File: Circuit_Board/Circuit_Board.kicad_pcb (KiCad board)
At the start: 2 copper layers, 17 parts, among them J1 Conn_01x02, J2 Control stuff, J3 Power stuff, J4 Conn_02x06_Odd_Even, U1 Pico

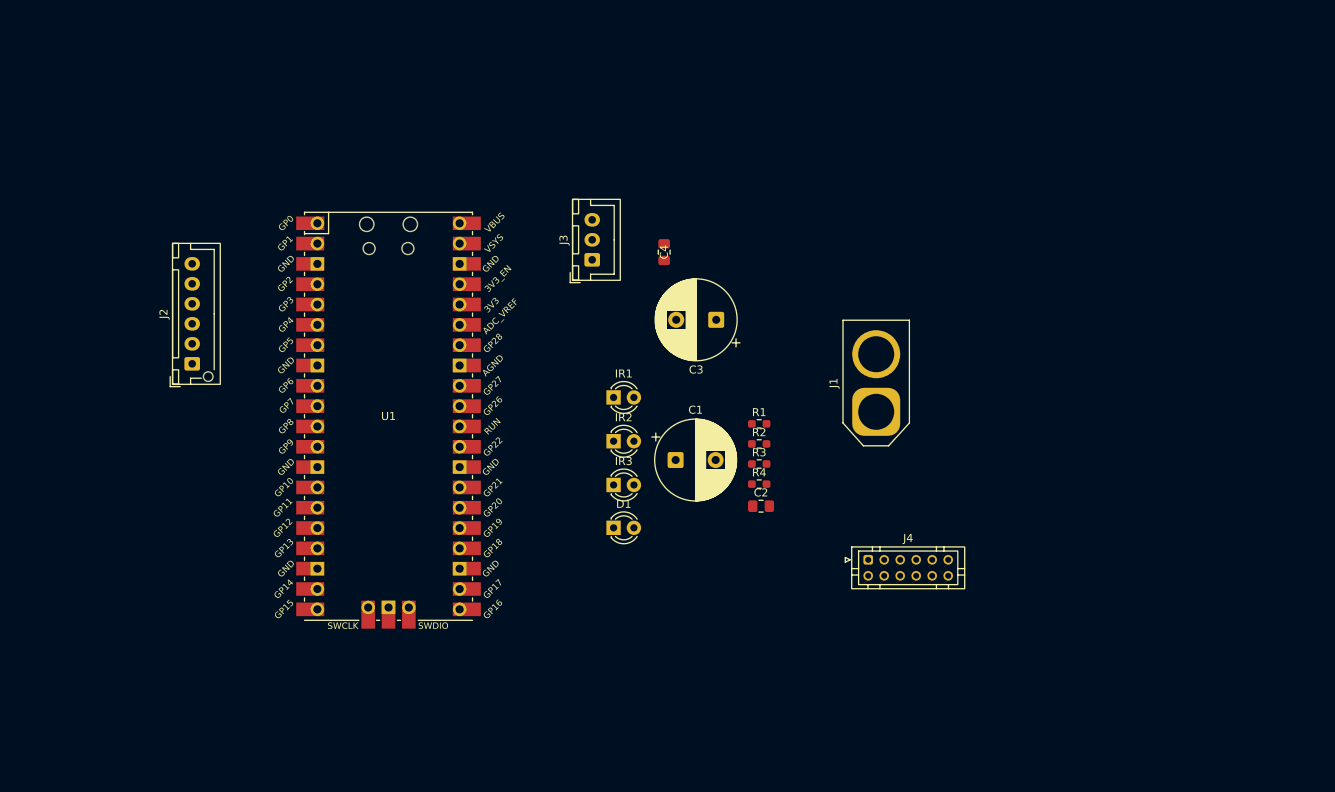
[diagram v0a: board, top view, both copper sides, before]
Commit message: Started work on pcb lay and add input pins vars to main
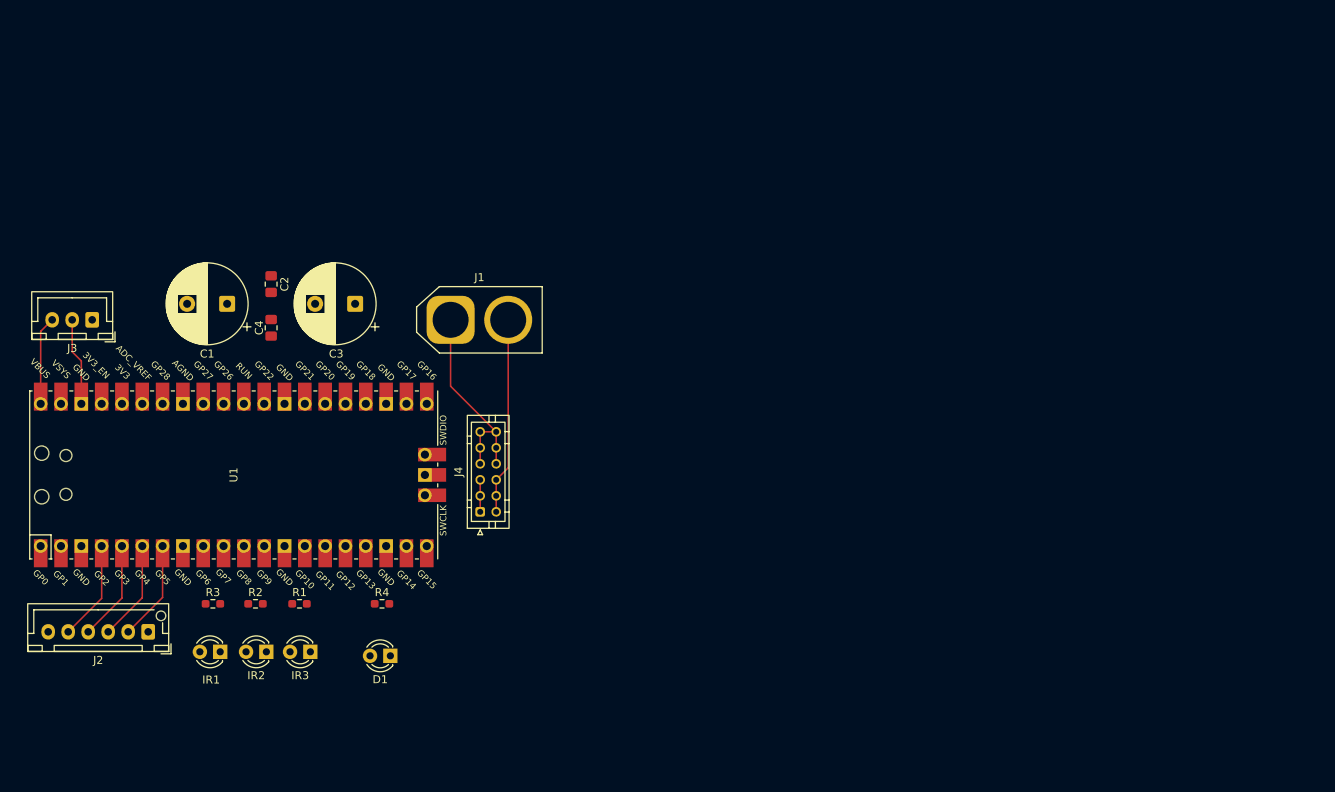
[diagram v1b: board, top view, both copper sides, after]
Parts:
- moved R3 70.5 mm to (83.1, 122.5)
- moved C2 67.2 mm to (90.4, 82.5), turned to -90 degrees
- moved R2 66.1 mm to (88.4, 122.5)
- moved J3 62.9 mm to (68.0, 87.0), turned to 180 degrees
- moved R1 61.7 mm to (93.9, 122.5)
- moved C1 59.4 mm to (84.9, 85.0), turned to 180 degrees
- moved IR1 58.6 mm to (84.0, 128.5), turned to 180 degrees
- moved J1 54.4 mm to (112.8, 87.0), turned to 0 degrees
- moved IR2 50.8 mm to (89.8, 128.5), turned to 180 degrees
- moved C4 50.0 mm to (90.4, 88.0), turned to -90 degrees
- moved R4 49.5 mm to (104.2, 122.5)
- moved J4 48.9 mm to (116.5, 111.0), turned to 90 degrees
- moved C3 45.2 mm to (100.9, 85.0)
- moved IR3 43.3 mm to (95.3, 128.5), turned to 180 degrees
- moved J2 33.9 mm to (75.0, 126.0), turned to 180 degrees
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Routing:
- net GND: track 0.00 -> 37.3 mm
- net +6V: track 0.00 -> 24.6 mm
- net Net-(J2-Pin_2): track 0.00 -> 12.5 mm
- net Net-(J2-Pin_3): track 0.00 -> 12.5 mm
- net Net-(J2-Pin_4): track 0.00 -> 12.5 mm
- net Net-(J2-Pin_5): track 0.00 -> 12.5 mm
- net VBUS: track 0.00 -> 11.1 mm
- net VCC: track 0.00 -> 4.00 mm

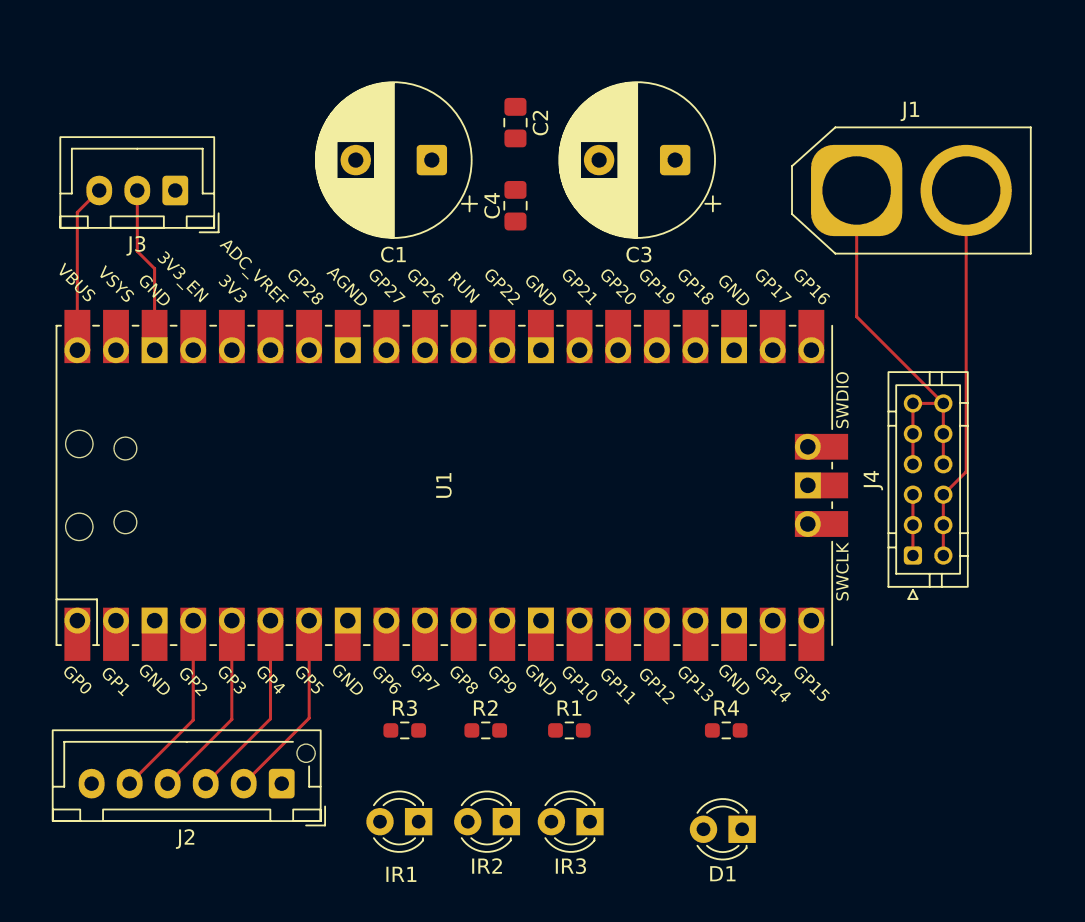
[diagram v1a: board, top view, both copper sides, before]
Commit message: Fix footprint error and 'finished' tras routing
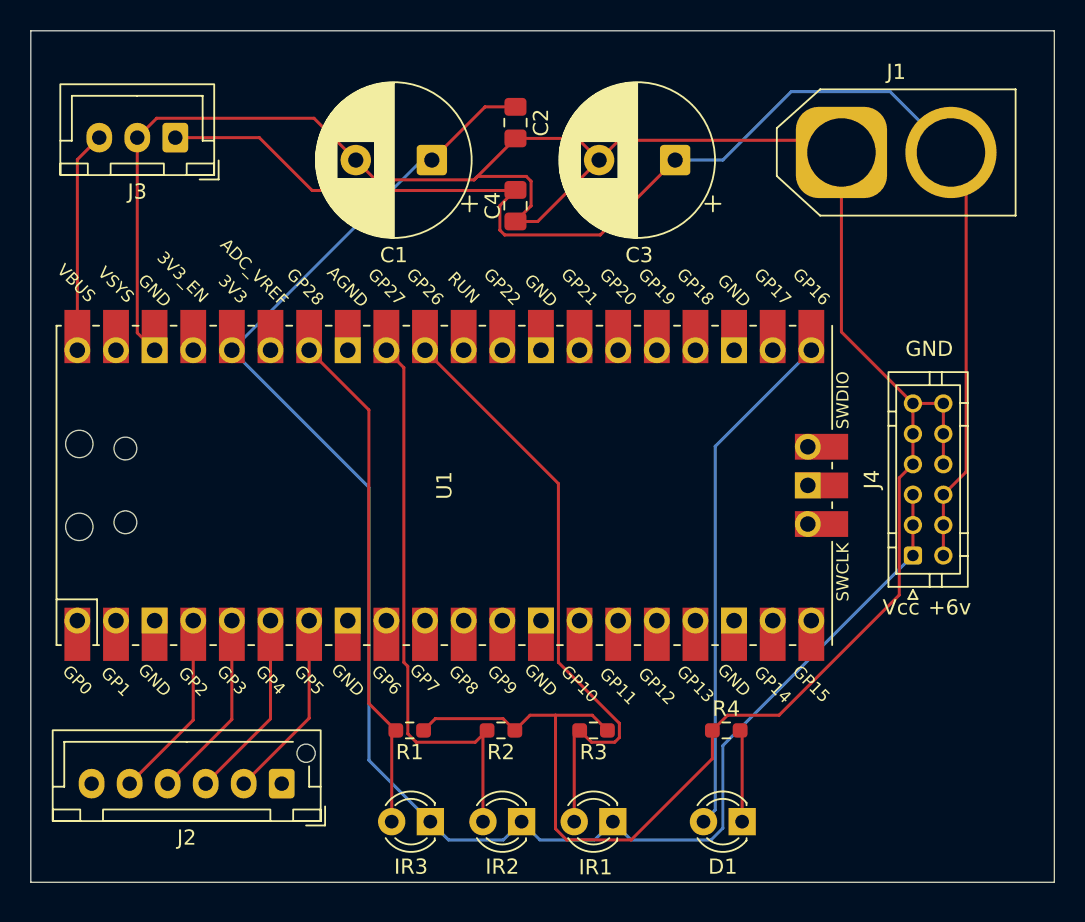
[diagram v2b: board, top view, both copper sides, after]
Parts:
- moved IR1 12.8 mm to (96.8, 128.5)
- moved R3 12.4 mm to (95.5, 122.5), turned to 180 degrees
- moved IR3 10.5 mm to (84.8, 128.5)
- moved R1 10.5 mm to (83.4, 122.5), turned to 180 degrees
- moved J3 3.47 mm to (68.0, 83.5)
- moved J1 2.69 mm to (111.8, 84.5)
- moved IR2 1.00 mm to (90.8, 128.5)
- moved R2 1.00 mm to (89.4, 122.5), turned to 180 degrees
- moved D1 0.50 mm to (105.3, 128.5)
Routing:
- net GND: track 37.3 -> 168.9 mm
- net VCC: track 4.00 -> 110.8 mm
- net +6V: track 24.6 -> 89.8 mm
- net Net-(U1-GPIO26_ADC0): track 0.00 -> 40.0 mm
- net Net-(U1-GPIO27_ADC1): track 0.00 -> 37.7 mm
- net Net-(D1-A): track 0.00 -> 33.9 mm
- net Net-(U1-GPIO28_ADC2): track 0.00 -> 33.5 mm
- net Net-(D1-K): track 0.00 -> 6.05 mm
- net VBUS: track 11.1 -> 14.6 mm
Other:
- board outline added: 67.3 x 56 mm
- board text added: "+6v"
- board text added: "GND"
- board text added: "Vcc"

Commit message: Changed board design
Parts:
- added D2: LED, LED_SMD:LED_0603_1608Metric_Pad1.05x0.95mm_HandSolder, F.Cu at (117.6, 119.2)
- added D3: LED, LED_SMD:LED_0603_1608Metric_Pad1.05x0.95mm_HandSolder, F.Cu at (117.6, 114.2)
- added D4: LED, LED_SMD:LED_0603_1608Metric_Pad1.05x0.95mm_HandSolder, F.Cu at (117.6, 109.2)
- added J5: Conn_01x20_Socket, Connector_PinSocket_2.54mm:PinSocket_1x20_P2.54mm_Vertical, F.Cu at (130.9, 71.2)
- added J6: Conn_01x20_Socket, Connector_PinSocket_2.54mm:PinSocket_1x20_P2.54mm_Vertical, F.Cu at (167.1, 71.4)
- added J7: Conn_01x04_Socket, Connector_JST:JST_XH_B4B-XH-A_1x04_P2.50mm_Vertical, F.Cu at (184.6, 123.7)
- added J8: Conn_01x04_Socket, Connector_JST:JST_XH_B4B-XH-A_1x04_P2.50mm_Vertical, F.Cu at (184.6, 106.7)
- added R5: R, Resistor_SMD:R_0603_1608Metric_Pad0.98x0.95mm_HandSolder, F.Cu at (123.5, 109.2)
- added R6: R, Resistor_SMD:R_0603_1608Metric_Pad0.98x0.95mm_HandSolder, F.Cu at (123.5, 114.2)
- added R7: R, Resistor_SMD:R_0603_1608Metric_Pad0.98x0.95mm_HandSolder, F.Cu at (123.5, 119.4)
- added SW1: SW_Push, Button_Switch_SMD:SW_Push_1P1T_NO_Vertical_Wuerth_434133025816, F.Cu at (120.4, 89.9)
- added SW2: SW_Push, Button_Switch_SMD:SW_Push_1P1T_NO_Vertical_Wuerth_434133025816, F.Cu at (120.4, 100.4)
- moved IR3 113.8 mm to (183.5, 71.8), turned to 0 degrees
- moved IR2 104.7 mm to (183.5, 79.8), turned to 0 degrees
- moved R1 101.6 mm to (174.4, 77.3), turned to 90 degrees
- moved IR1 95.8 mm to (183.5, 87.8), turned to 0 degrees
- moved C1 94.6 mm to (169.9, 126.4), turned to -90 degrees
- moved R2 94.2 mm to (174.4, 81.8), turned to 90 degrees
- moved R3 86.8 mm to (174.4, 86.3), turned to 90 degrees
- moved D1 84.7 mm to (183.4, 95.8), turned to 0 degrees
- moved C2 84.0 mm to (160.4, 129.0)
- moved R4 76.9 mm to (174.3, 90.8), turned to 90 degrees
- moved U1 64.1 mm to (148.9, 95.4), turned to 0 degrees
- moved C4 62.4 mm to (137.4, 129.0)
- moved J3 51.7 mm to (107.4, 116.9), turned to 90 degrees
- moved C3 50.0 mm to (128.9, 126.4), turned to -90 degrees
- moved J1 45.1 mm to (115.9, 129.4), turned to 180 degrees
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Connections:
- U1 pad 1: unconnected-(U1-GPIO0-Pad1) -> Net-(J5-Pin_1)
- U1 pad 10: unconnected-(U1-GPIO7-Pad10) -> Net-(J5-Pin_10)
- U1 pad 11: unconnected-(U1-GPIO8-Pad11) -> Net-(J5-Pin_11)
- U1 pad 12: unconnected-(U1-GPIO9-Pad12) -> Net-(J5-Pin_12)
- U1 pad 13: unconnected-(U1-GND-Pad13) -> Net-(J5-Pin_13)
- U1 pad 14: unconnected-(U1-GPIO10-Pad14) -> Net-(J5-Pin_14)
- U1 pad 15: unconnected-(U1-GPIO11-Pad15) -> Net-(J5-Pin_15)
- U1 pad 16: unconnected-(U1-GPIO12-Pad16) -> Net-(J5-Pin_16)
- U1 pad 17: unconnected-(U1-GPIO13-Pad17) -> Net-(J5-Pin_17)
- U1 pad 18: unconnected-(U1-GND-Pad18) -> Net-(J5-Pin_18)
- U1 pad 19: unconnected-(U1-GPIO14-Pad19) -> Net-(J5-Pin_19)
- U1 pad 2: unconnected-(U1-GPIO1-Pad2) -> Net-(J5-Pin_2)
- U1 pad 20: unconnected-(U1-GPIO15-Pad20) -> Net-(J5-Pin_20)
- U1 pad 21: Net-(D1-A) -> Net-(J6-Pin_20)
- U1 pad 22: unconnected-(U1-GPIO17-Pad22) -> Net-(J6-Pin_19)
- U1 pad 23: unconnected-(U1-GND-Pad23) -> Net-(J6-Pin_18)
- U1 pad 24: unconnected-(U1-GPIO18-Pad24) -> Net-(J6-Pin_17)
- U1 pad 25: unconnected-(U1-GPIO19-Pad25) -> Net-(J6-Pin_16)
- U1 pad 26: unconnected-(U1-GPIO20-Pad26) -> Net-(J6-Pin_15)
- U1 pad 27: unconnected-(U1-GPIO21-Pad27) -> Net-(D1-A)
- U1 pad 28: unconnected-(U1-GND-Pad28) -> Net-(J6-Pin_13)
- U1 pad 29: unconnected-(U1-GPIO22-Pad29) -> Net-(J6-Pin_12)
- U1 pad 3: unconnected-(U1-GND-Pad3) -> Net-(J5-Pin_3)
- U1 pad 30: unconnected-(U1-RUN-Pad30) -> Net-(J6-Pin_11)
- U1 pad 33: unconnected-(U1-AGND-Pad33) -> Net-(J6-Pin_8)
- U1 pad 35: unconnected-(U1-ADC_VREF-Pad35) -> Net-(J6-Pin_6)
- U1 pad 37: unconnected-(U1-3V3_EN-Pad37) -> Net-(J6-Pin_4)
- U1 pad 39: unconnected-(U1-VSYS-Pad39) -> Net-(J6-Pin_2)
- U1 pad 8: unconnected-(U1-GND-Pad8) -> Net-(J5-Pin_8)
- U1 pad 9: unconnected-(U1-GPIO6-Pad9) -> Net-(J5-Pin_9)
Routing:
- net VBUS: track 14.6 -> 103.7 mm
- net VCC: track 110.8 -> 166.7 mm
- net Net-(J5-Pin_15): track 0.00 -> 31.8 mm
- net Net-(J6-Pin_19): track 0.00 -> 30.7 mm
- net Net-(J6-Pin_20): track 0.00 -> 30.7 mm
- net GND: track 168.9 -> 198.0 mm
- net +6V: track 89.8 -> 61.4 mm
- net Net-(J6-Pin_17): track 0.00 -> 27.1 mm
- net Net-(J6-Pin_16): track 0.00 -> 27.1 mm
- net Net-(J5-Pin_16): track 0.00 -> 25.4 mm
- net Net-(J2-Pin_5): track 12.5 -> 37.9 mm
- net Net-(J2-Pin_4): track 12.5 -> 37.9 mm
- net Net-(J2-Pin_3): track 12.5 -> 37.8 mm
- net Net-(J2-Pin_2): track 12.5 -> 37.8 mm
- net Net-(J6-Pin_9): track 37.7 -> 59.0 mm
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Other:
- board size 67.3 x 56 mm -> 87 x 69 mm

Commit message: v1.0 of board excluding the mounting holes
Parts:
- added C5: C_Polarized, Capacitor_SMD:C_0805_2012Metric_Pad1.18x1.45mm_HandSolder, F.Cu at (171.4, 76.0)
- added C6: C_Polarized, Capacitor_SMD:C_0805_2012Metric_Pad1.18x1.45mm_HandSolder, F.Cu at (171.4, 70.9)
- added C7: C_Polarized, Capacitor_SMD:C_0805_2012Metric_Pad1.18x1.45mm_HandSolder, F.Cu at (107.7, 107.2)
- added C8: C_Polarized, Capacitor_SMD:C_0805_2012Metric_Pad1.18x1.45mm_HandSolder, F.Cu at (107.7, 121.9)
- added H1: MountingHole, MountingHole:MountingHole_3.2mm_M3, F.Cu at (219.7, 90.2)
- added H2: MountingHole, MountingHole:MountingHole_3.2mm_M3, F.Cu at (219.7, 121.9)
- added H3: MountingHole, MountingHole:MountingHole_3.2mm_M3, F.Cu at (217.5, 101.3)
- added H4: MountingHole, MountingHole:MountingHole_3.2mm_M3, F.Cu at (217.5, 109.2)
- added J9: LED_AMP, Connector_JST:JST_XH_B4B-XH-A_1x04_P2.50mm_Vertical, F.Cu at (176.5, 106.0)
- added Q2: IRF540N, Package_TO_SOT_THT:TO-220-3_Vertical, F.Cu at (185.1, 107.3)
- added R8: R, Resistor_SMD:R_0603_1608Metric_Pad0.98x0.95mm_HandSolder, F.Cu at (181.0, 109.5)
- added SW3: SW_Push, Button_Switch_SMD:SW_Push_1P1T_NO_E-Switch_TL3301NxxxxxG, F.Cu at (119.9, 104.8)
- J2: footprint Connector_JST:JST_XH_B6B-XH-AM_1x06_P2.50mm_Vertical -> Connector_JST:JST_XH_B6B-XH-A_1x06_P2.50mm_Vertical
- J7: value Conn_01x04_Socket -> GPIO_1
- J8: value Conn_01x04_Socket -> GPIO_2
- SW1, SW2: footprint Button_Switch_SMD:SW_Push_1P1T_NO_Vertical_Wuerth_434133025816 -> Button_Switch_SMD:SW_Push_1P1T_NO_E-Switch_TL3301NxxxxxG
- moved J8 18.5 mm to (176.5, 123.3)
- moved SW2 4.91 mm to (120.0, 95.5), turned to 180 degrees
- moved SW1 3.61 mm to (119.9, 86.4), turned to 180 degrees
- moved C1 3.56 mm to (166.4, 126.4)
- moved D4 3.20 mm to (117.8, 112.4)
- moved R5 3.19 mm to (123.5, 112.4)
- moved J5 2.98 mm to (128.3, 69.8)
- moved C2 2.97 mm to (157.5, 129.3)
- moved D3 2.65 mm to (117.9, 116.8)
- moved IR1 2.57 mm to (186.1, 87.6), turned to 180 degrees
- moved IR2 2.56 mm to (186.1, 79.8), turned to 180 degrees
- moved IR3 2.56 mm to (186.1, 71.8), turned to 180 degrees
- moved R6 2.54 mm to (123.5, 116.8)
- moved D2 2.10 mm to (117.9, 121.3)
- moved U1 2.09 mm to (147.3, 94.0)
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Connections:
- net Net-(J6-Pin_15) renamed /FET_GATE
- J2 pad 1: unconnected-(J2-Pin_1-Pad1) -> Net-(J2-Pin_1)
- J2 pad 6: unconnected-(J2-Pin_6-Pad6) -> Net-(J2-Pin_6)
- J5 pad 10: Net-(J5-Pin_10) -> Net-(J2-Pin_1)
- J5 pad 4: Net-(J2-Pin_5) -> Net-(J2-Pin_6)
- J5 pad 5: Net-(J2-Pin_4) -> Net-(J2-Pin_5)
- J5 pad 6: Net-(J2-Pin_3) -> Net-(J2-Pin_4)
- J5 pad 7: Net-(J2-Pin_2) -> Net-(J2-Pin_3)
- J5 pad 9: Net-(J5-Pin_9) -> Net-(J2-Pin_2)
- SW1 pad 1: Net-(SW1-Pad1) -> GND
- SW1 pad 2: Net-(J5-Pin_15) -> Net-(J5-Pin_14)
- SW2 pad 1: Net-(SW1-Pad1) -> GND
- SW2 pad 2: Net-(J5-Pin_16) -> Net-(J5-Pin_15)
- U1 pad 10: Net-(J5-Pin_10) -> Net-(J2-Pin_1)
- U1 pad 4: Net-(J2-Pin_5) -> Net-(J2-Pin_6)
- U1 pad 5: Net-(J2-Pin_4) -> Net-(J2-Pin_5)
- U1 pad 6: Net-(J2-Pin_3) -> Net-(J2-Pin_4)
- U1 pad 7: Net-(J2-Pin_2) -> Net-(J2-Pin_3)
- U1 pad 9: Net-(J5-Pin_9) -> Net-(J2-Pin_2)
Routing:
- net VCC: track 166.7 -> 23.4 mm, vias 0 -> 2
- net GND: track 198.0 -> 112.6 mm, vias 0 -> 14
- net VBUS: track 103.7 -> 151.8 mm
- net Net-(J2-Pin_6): track 0.00 -> 35.8 mm
- net Net-(J2-Pin_1): track 0.00 -> 34.7 mm
- net Net-(J5-Pin_14): track 9.07 -> 39.6 mm
- net Net-(J6-Pin_9): track 59.0 -> 31.6 mm
- net /FET_GATE: track 9.44 -> 34.9 mm
- net Net-(J6-Pin_7): track 49.7 -> 32.8 mm
- net Net-(SW1-Pad1): track 14.6 -> 0.00 mm
- net Net-(J6-Pin_10): track 43.8 -> 31.2 mm
- net Net-(J9-Pin_4): track 0.00 -> 10.1 mm
- net Net-(J5-Pin_9): track 9.07 -> 0.00 mm
- net Net-(J5-Pin_10): track 9.07 -> 0.00 mm
- net Net-(J6-Pin_20): track 30.7 -> 39.2 mm
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- added copper zone on In2.Cu, net +6V
- added copper zone on In1.Cu, net GND
- added copper zone on In2.Cu, net VCC
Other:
- board size 87 x 69 mm -> 90.2 x 71.9 mm
- copper layers 2 -> 4
- board text added: "Designed by: Jense Daurt Patrick Leiser v1.0"
- board text added: "Sierra College Robotics Club Swarm Bots"
- board text added: "Spring 2026"
